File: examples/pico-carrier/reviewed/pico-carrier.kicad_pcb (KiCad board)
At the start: 2 copper layers, 80 x 56 mm, 9 parts, among them J1 5V IN, J3 GP0-GP15, J4 GP16-GP28, PWR, U1 Pico

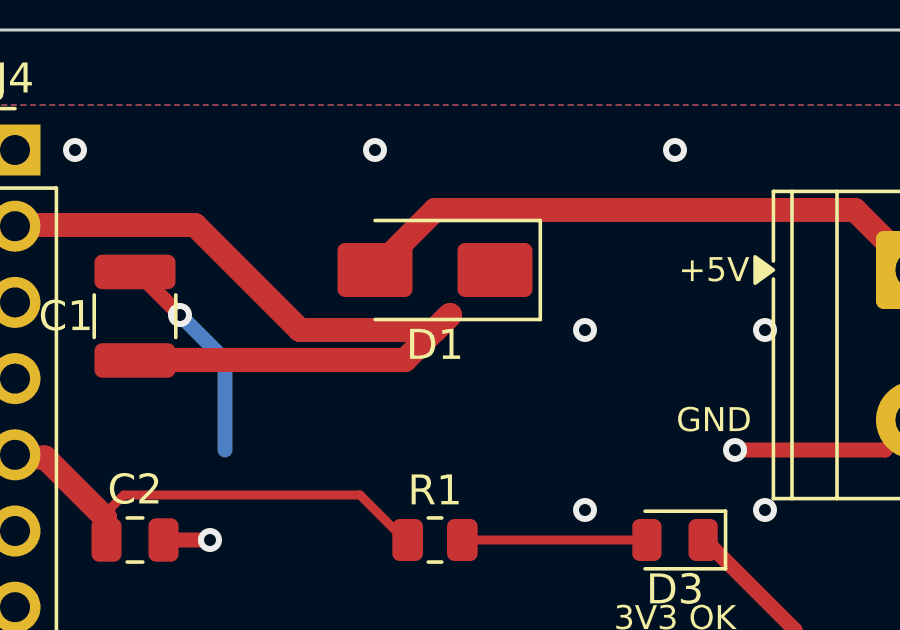
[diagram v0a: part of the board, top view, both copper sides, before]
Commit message: Never cut a corner off the pad it was there to reach
Once two routes meeting at a pad are merged into one run, the pad is an
interior corner of a polyline like any other, and the chamfer cut it -
moving the copper off the pad and leaving the net unconnected, which is
not something you can see in the shape. Both clean-up passes now hold
every pad and every track end still, from one list, for the same reason:
copper that something else is joined to is not theirs to move.

That is the last of the unconnected-net errors on the buck, the motor
and the opamp boards, and the 0 degree spur on the Pico's VSYS - which
was the failed half of a route to a pad the chamfer had already cut it
away from.
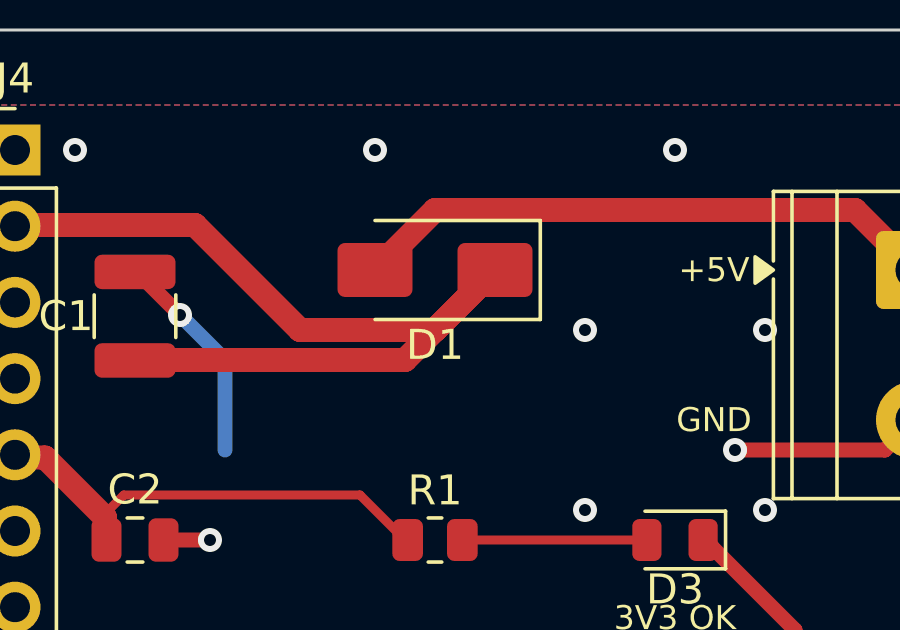
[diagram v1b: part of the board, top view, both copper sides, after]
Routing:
- net /VSYS: track 33.6 -> 37.9 mm
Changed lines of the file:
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@@
 	(segment (start 148.0 66.5) (end 151.5 70.0) (width 0.8) (layer "F.Cu") (net 36))
 	(segment (start 151.5 70.0) (end 156.0 70.0) (width 0.8) (layer "F.Cu") (net 36))
-	(segment (start 156.0 70.0) (end 156.5 69.5) (width 0.8) (layer "F.Cu") (net 36))
-	(segment (start 156.5 69.5) (end 155.0 71.0) (width 0.8) (layer "F.Cu") (net 36))
+	(segment (start 156.0 70.0) (end 158.0 68.0) (width 0.8) (layer "F.Cu") (net 36))
+	(segment (start 158.0 68.0) (end 155.0 71.0) (width 0.8) (layer "F.Cu") (net 36))
 	(segment (start 155.0 71.0) (end 146.25 71.0) (width 0.8) (layer "F.Cu") (net 36))
 	(segment (start 146.25 71.0) (end 146.235 71.015) (width 0.8) (layer "F.Cu") (net 36))
